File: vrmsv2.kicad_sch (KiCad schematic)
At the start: 5 parts

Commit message: Updated (?) subsheets
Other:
- moved on the sheet: D1, D2, D3, F1, R1

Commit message: Annotated schematic
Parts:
- renumbered D1 to D3, D2 to D4, D3 to D5, R1 to R15
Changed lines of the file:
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@@
   (symbol (lib_id "Device:D_Schottky") (at 114.3 82.55 180) (unit 1)
     (in_bom yes) (on_board yes) (fields_autoplaced)
-    (property "Reference" "D2" (id 0) (at 114.6175 78.74 0))
+    (property "Reference" "D4" (id 0) (at 114.6175 78.74 0))
     (property "Value" "0.7dV" (id 1) (at 114.6175 78.74 0)
       (effects (font (size 1.27 1.27)) hide)
@@
   (symbol (lib_id "power:+3V3") (at 186.69 73.66 0) (unit 1)
     (in_bom yes) (on_board yes) (fields_autoplaced)
-    (property "Reference" "#PWR0101" (id 0) (at 186.69 77.47 0)
+    (property "Reference" "#PWR044" (id 0) (at 186.69 77.47 0)
       (effects (font (size 1.27 1.27)) hide)
     )
@@
   (symbol (lib_id "power:+5V") (at 151.13 73.66 0) (unit 1)
     (in_bom yes) (on_board yes) (fields_autoplaced)
-    (property "Reference" "#PWR0102" (id 0) (at 151.13 77.47 0)
+    (property "Reference" "#PWR043" (id 0) (at 151.13 77.47 0)
       (effects (font (size 1.27 1.27)) hide)
     )
@@
   (symbol (lib_id "power:GND") (at 104.14 91.44 0) (unit 1)
     (in_bom yes) (on_board yes) (fields_autoplaced)
-    (property "Reference" "#PWR0103" (id 0) (at 104.14 97.79 0)
+    (property "Reference" "#PWR041" (id 0) (at 104.14 97.79 0)
       (effects (font (size 1.27 1.27)) hide)
     )
@@
   (symbol (lib_id "power:+24V") (at 86.36 82.55 0) (unit 1)
     (in_bom yes) (on_board yes) (fields_autoplaced)
-    (property "Reference" "#PWR0107" (id 0) (at 86.36 86.36 0)
+    (property "Reference" "#PWR040" (id 0) (at 86.36 86.36 0)
       (effects (font (size 1.27 1.27)) hide)
     )
@@
   (symbol (lib_id "Device:D_Zener") (at 104.14 86.36 270) (unit 1)
     (in_bom yes) (on_board yes) (fields_autoplaced)
-    (property "Reference" "D1" (id 0) (at 106.68 85.0899 90)
+    (property "Reference" "D3" (id 0) (at 106.68 85.0899 90)
       (effects (font (size 1.27 1.27)) (justify left))
     )
@@
   (symbol (lib_id "Device:LED") (at 119.38 90.17 90) (unit 1)
     (in_bom yes) (on_board yes) (fields_autoplaced)
-    (property "Reference" "D3" (id 0) (at 123.19 90.4874 90)
+    (property "Reference" "D5" (id 0) (at 123.19 90.4874 90)
       (effects (font (size 1.27 1.27)) (justify right))
     )
@@
   (symbol (lib_id "Device:R") (at 119.38 97.79 180) (unit 1)
     (in_bom yes) (on_board yes)
-    (property "Reference" "R1" (id 0) (at 121.92 97.79 90))
+    (property "Reference" "R15" (id 0) (at 121.92 97.79 90))
     (property "Value" "470R" (id 1) (at 124.46 97.79 90))
     (property "Footprint" "Resistor_SMD:R_0603_1608Metric_Pad0.98x0.95mm_HandSolder" (id 2) (at 121.158 97.79 90)
@@
   (symbol (lib_id "power:GND") (at 119.38 101.6 0) (unit 1)
     (in_bom yes) (on_board yes) (fields_autoplaced)
-    (property "Reference" "#PWR0108" (id 0) (at 119.38 107.95 0)
+    (property "Reference" "#PWR042" (id 0) (at 119.38 107.95 0)
       (effects (font (size 1.27 1.27)) hide)
     )

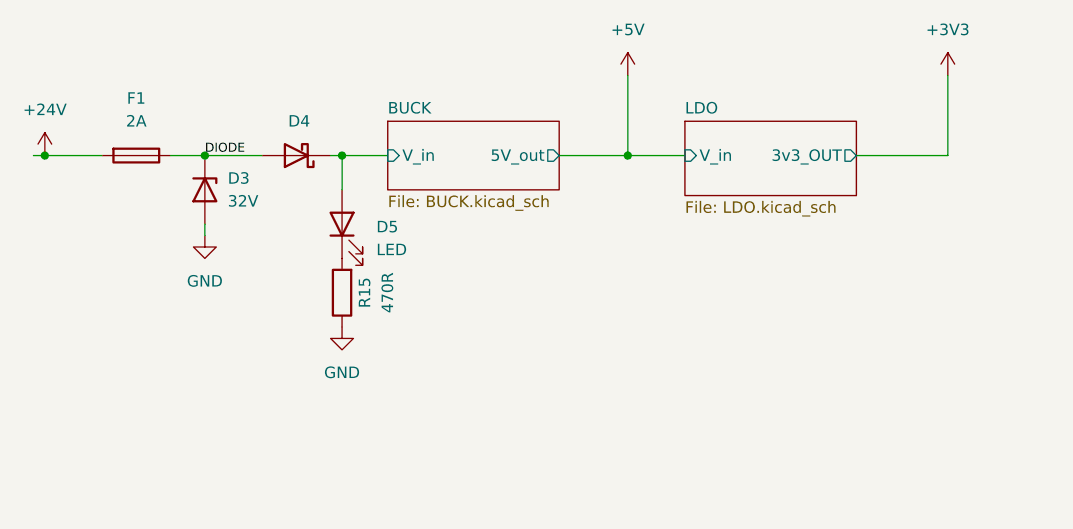
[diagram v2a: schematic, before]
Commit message: Added 0 Ω resistor to shield, grounded it, reannotated schematic, reassigned some footprints
Starting layout
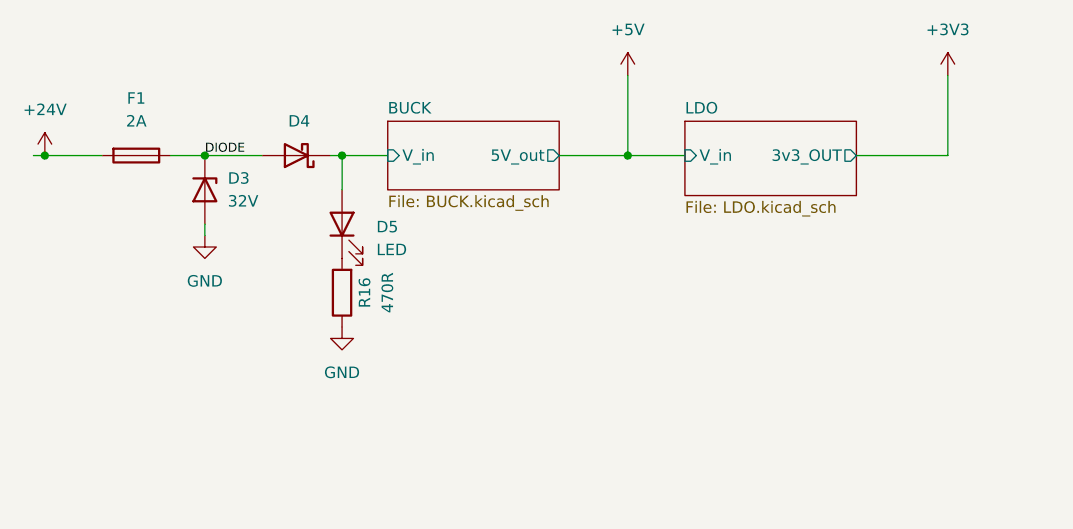
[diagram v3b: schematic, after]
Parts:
- D4: footprint Diode_SMD:D_SMA -> Diode_SMD:D_SMA_Handsoldering
- renumbered R15 to R16
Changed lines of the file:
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@@
       (effects (font (size 1.27 1.27)) hide)
     )
-    (property "Footprint" "Diode_SMD:D_SMA" (id 2) (at 114.3 82.55 0)
+    (property "Footprint" "Diode_SMD:D_SMA_Handsoldering" (id 2) (at 114.3 82.55 0)
       (effects (font (size 1.27 1.27)) hide)
     )
@@
   (symbol (lib_id "power:+3V3") (at 186.69 73.66 0) (unit 1)
     (in_bom yes) (on_board yes) (fields_autoplaced)
-    (property "Reference" "#PWR044" (id 0) (at 186.69 77.47 0)
+    (property "Reference" "#PWR050" (id 0) (at 186.69 77.47 0)
       (effects (font (size 1.27 1.27)) hide)
     )
@@
   (symbol (lib_id "power:+5V") (at 151.13 73.66 0) (unit 1)
     (in_bom yes) (on_board yes) (fields_autoplaced)
-    (property "Reference" "#PWR043" (id 0) (at 151.13 77.47 0)
+    (property "Reference" "#PWR049" (id 0) (at 151.13 77.47 0)
       (effects (font (size 1.27 1.27)) hide)
     )
@@
   (symbol (lib_id "power:GND") (at 104.14 91.44 0) (unit 1)
     (in_bom yes) (on_board yes) (fields_autoplaced)
-    (property "Reference" "#PWR041" (id 0) (at 104.14 97.79 0)
+    (property "Reference" "#PWR047" (id 0) (at 104.14 97.79 0)
       (effects (font (size 1.27 1.27)) hide)
     )
@@
   (symbol (lib_id "power:+24V") (at 86.36 82.55 0) (unit 1)
     (in_bom yes) (on_board yes) (fields_autoplaced)
-    (property "Reference" "#PWR040" (id 0) (at 86.36 86.36 0)
+    (property "Reference" "#PWR046" (id 0) (at 86.36 86.36 0)
       (effects (font (size 1.27 1.27)) hide)
     )
@@
   (symbol (lib_id "Device:R") (at 119.38 97.79 180) (unit 1)
     (in_bom yes) (on_board yes)
-    (property "Reference" "R15" (id 0) (at 121.92 97.79 90))
+    (property "Reference" "R16" (id 0) (at 121.92 97.79 90))
     (property "Value" "470R" (id 1) (at 124.46 97.79 90))
     (property "Footprint" "Resistor_SMD:R_0603_1608Metric_Pad0.98x0.95mm_HandSolder" (id 2) (at 121.158 97.79 90)
@@
   (symbol (lib_id "power:GND") (at 119.38 101.6 0) (unit 1)
     (in_bom yes) (on_board yes) (fields_autoplaced)
-    (property "Reference" "#PWR042" (id 0) (at 119.38 107.95 0)
+    (property "Reference" "#PWR048" (id 0) (at 119.38 107.95 0)
       (effects (font (size 1.27 1.27)) hide)
     )
